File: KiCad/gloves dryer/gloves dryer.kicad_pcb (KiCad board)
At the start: 2 copper layers, 36 x 40 mm, 21 parts, among them J1 Conn_01x03, J4 PJ-114AH-SMT-TR, J5 Conn_01x02, J6 Conn_01x05, J7 Conn_01x02, Q1 PN2222A, Q2 PN2222A, SW1 SW_Push_Dual, SW2 SW_Push_Dual, U1 PIC16F18126-I/P, U2 AMS1117-5.0

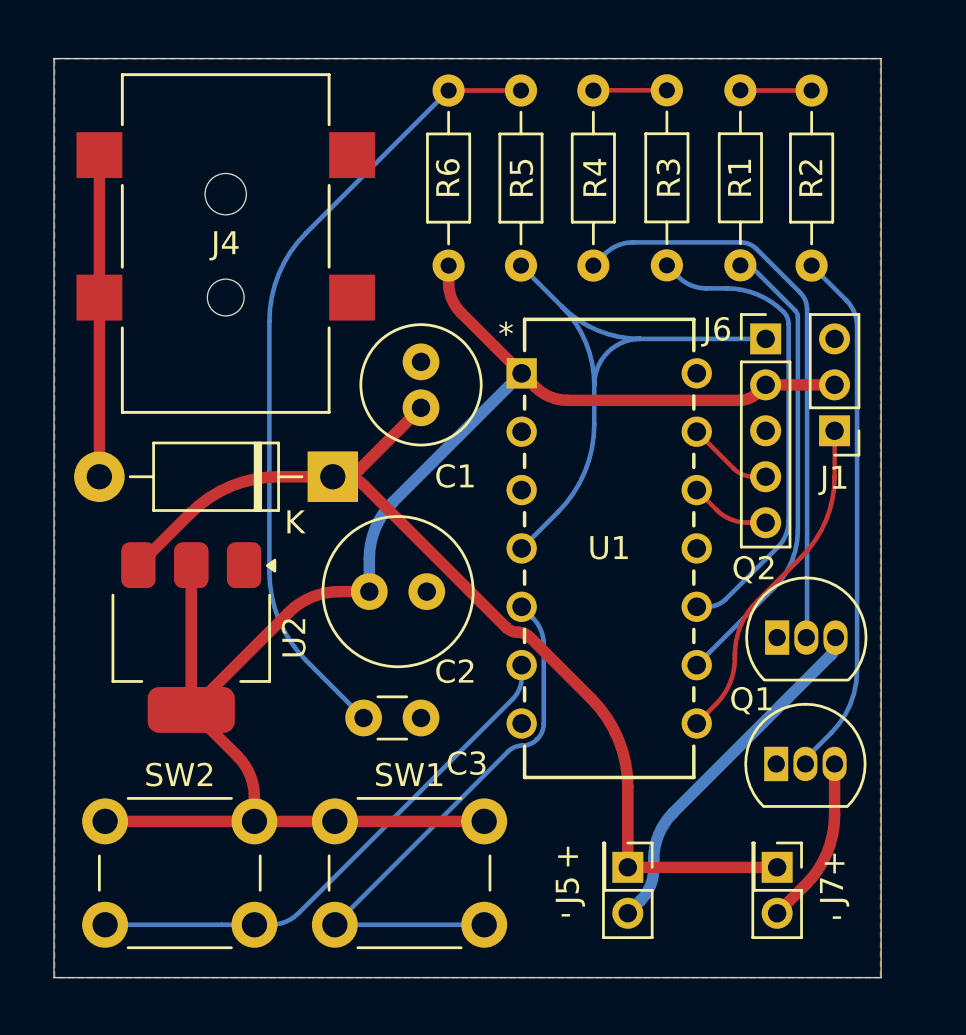
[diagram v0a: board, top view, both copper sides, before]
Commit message: Finished PCB, working on firmware for added switch state
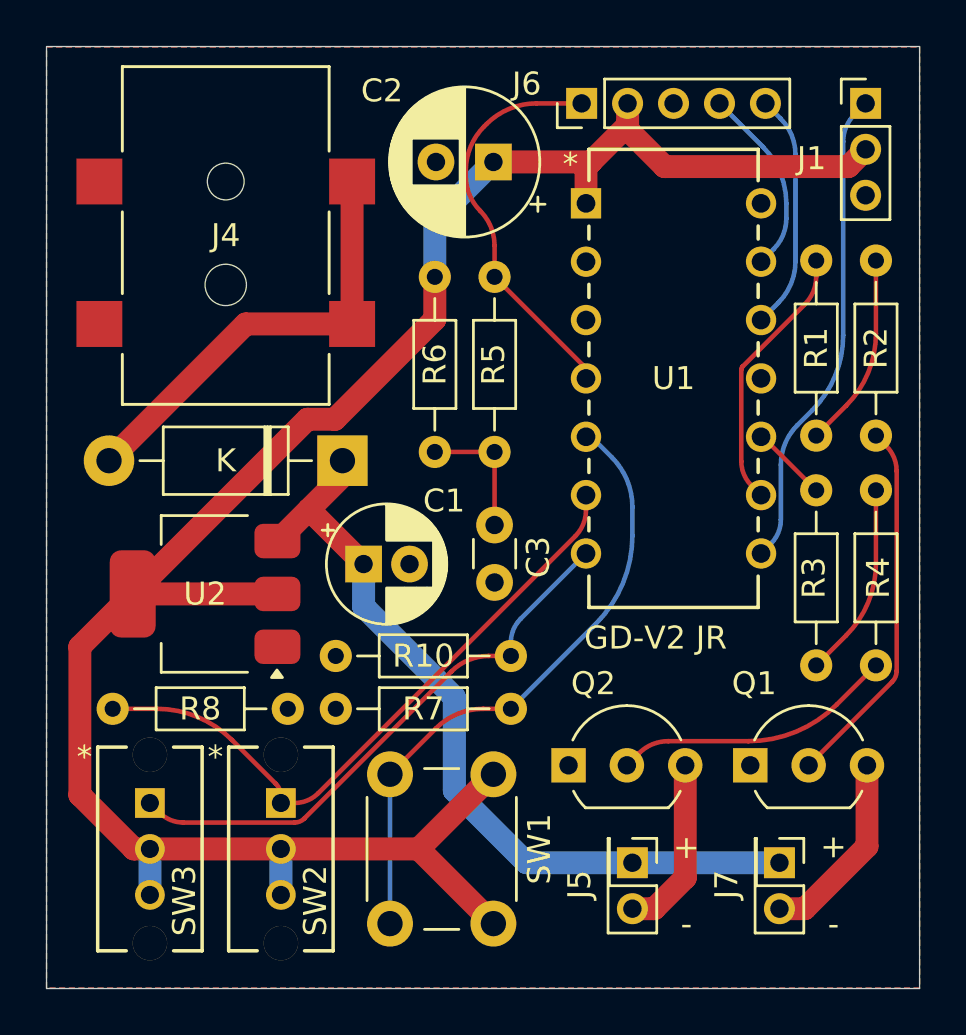
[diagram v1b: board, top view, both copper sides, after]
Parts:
- added R10: 10k, Resistor_THT:R_Axial_DIN0204_L3.6mm_D1.6mm_P7.62mm_Horizontal, F.Cu at (173.8, 76.8)
- added R7: 10k, Resistor_THT:R_Axial_DIN0204_L3.6mm_D1.6mm_P7.62mm_Horizontal, F.Cu at (173.8, 79.1)
- added R8: 10k, Resistor_THT:R_Axial_DIN0204_L3.6mm_D1.6mm_P7.62mm_Horizontal, F.Cu at (171.7, 79.1)
- added SW3: OS102011MS2QN1, OS102011MS2QN1:SPDT_OS102011_CNK, F.Cu at (165.7, 83.2)
- C1: footprint Capacitor_THT:C_Radial_D5.0mm_H11.0mm_P2.00mm -> Capacitor_THT:CP_Radial_D5.0mm_P2.00mm
- C2: footprint Capacitor_THT:C_Radial_D6.3mm_H11.0mm_P2.50mm -> Capacitor_THT:CP_Radial_D6.3mm_P2.50mm
- Q1, Q2: footprint Package_TO_SOT_THT:TO-92_Inline -> Package_TO_SOT_THT:TO-92_Inline_Wide
- SW2: value SW_Push_Dual -> OS102011MS2QN1; footprint Button_Switch_THT:SW_PUSH_6mm_H5mm -> OS102011MS2QN1:SPDT_OS102011_CNK
- moved R4 21.3 mm to (197.3, 69.6)
- moved C2 19.5 mm to (180.7, 55.3), turned to 180 degrees
- moved R5 15.8 mm to (180.7, 67.9), turned to 90 degrees
- moved R6 15.7 mm to (178.1, 67.9), turned to 90 degrees
- moved J1 14.3 mm to (196.8, 52.8), turned to 0 degrees
- moved J6 13.0 mm to (184.5, 52.8), turned to 90 degrees
- moved R3 11.8 mm to (194.7, 69.6), turned to -90 degrees
- moved Q2 10.6 mm to (183.9, 81.6)
- moved C3 10.2 mm to (180.7, 71.1), turned to -90 degrees
- moved R2 7.91 mm to (197.3, 59.6)
- moved U1 7.91 mm to (184.7, 57.1)
- moved SW2 7.69 mm to (171.4, 83.2)
- moved C1 7.24 mm to (175.0, 72.8), turned to 0 degrees
- moved SW1 7.20 mm to (180.6, 82.0), turned to -90 degrees
- moved R1 3.31 mm to (194.7, 59.6), turned to -90 degrees
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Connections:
- SW2 pad 1: /VDD_5V -> /SW1
- SW2 pad 2: /BT2 -> /VDD_5V
- U1 pad 6: /BT2 -> /SW1
- U1 pad 7: unconnected-(U1-RC3-Pad7) -> /SW2
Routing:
- net Net-(C3-Pad1): track 34.9 -> 5.78 mm
- net /SW1: track 0.00 -> 28.4 mm
- net /SW2: track 0.00 -> 24.6 mm
- net /BT2: track 23.3 -> 0.00 mm
- net /VDD_5V: track 70.6 -> 91.8 mm
- net /IF1: track 20.6 -> 3.36 mm
- net Net-(Q2-B): track 25.3 -> 12.3 mm
- net /VDDG_12V: track 45.0 -> 35.0 mm
- net /MCLR: track 26.7 -> 17.6 mm
- net /IF2: track 20.3 -> 11.8 mm
- net /F1-: track 15.5 -> 7.75 mm
- net Net-(Q1-B): track 23.2 -> 16.2 mm
- net /CLK: track 3.50 -> 10.4 mm
- net /IO_SENS: track 14.7 -> 21.0 mm
- net /VDD_12V: track 14.2 -> 19.8 mm
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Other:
- board size 36 x 40 mm -> 38 x 41 mm
- board text added: "GD-V2 JR"

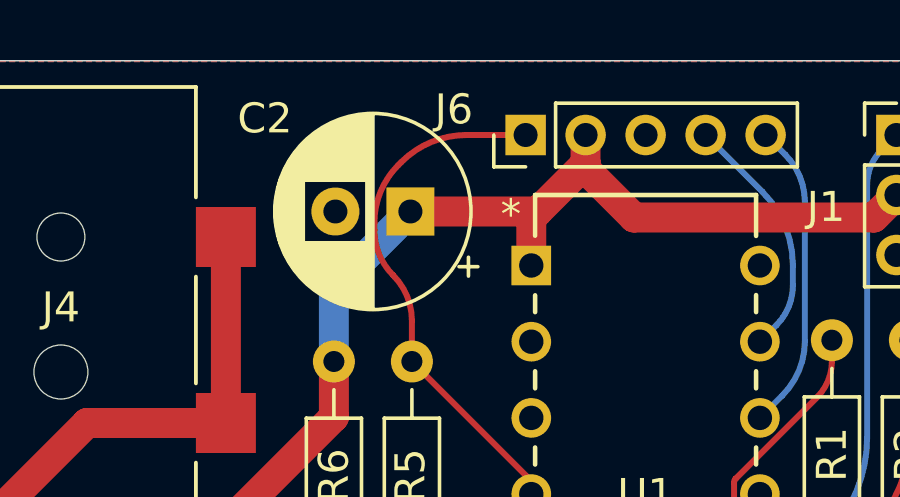
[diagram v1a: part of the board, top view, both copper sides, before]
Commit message: Updated firmware for version two of the project, as well as kicad file for version 2
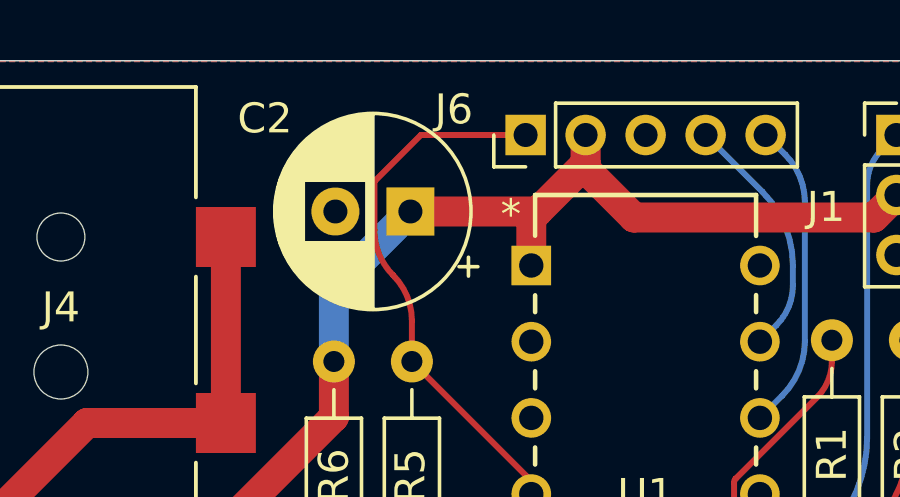
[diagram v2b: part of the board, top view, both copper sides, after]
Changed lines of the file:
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@@
 	)
 	(segment
-		(start 182.522792 52.75)
-		(end 184.49 52.75)
+		(start 181 52.75)
+		(end 179.45 54.3)
+		(width 0.2)
+		(layer "F.Cu")
+		(net 20)
+	)
+	(segment
+		(start 184.68 64.5)
+		(end 184.68 64.72)
 		(width 0.2)
 		(layer "F.Cu")
@@
 	)
 	(segment
-		(start 184.68 64.5)
-		(end 184.68 64.72)
+		(start 184.49 52.75)
+		(end 181 52.75)
 		(width 0.2)
 		(layer "F.Cu")
@@
 	)
 	(segment
-		(start 180.245495 53.754504)
-		(end 180.35 53.65)
-		(width 0.2)
-		(layer "F.Cu")
-		(net 20)
-	)
-	(segment
-		(start 179.45 55.916116)
-		(end 179.45 55.675)
+		(start 179.45 54.3)
+		(end 179.45 55.916116)
 		(width 0.2)
 		(layer "F.Cu")
@@
 	)
 	(arc
+		(start 180.075 57.425)
+		(mid 180.537567 58.117281)
+		(end 180.7 58.933883)
+		(width 0.2)
+		(layer "F.Cu")
+		(net 20)
+	)
+	(arc
 		(start 179.45 55.916116)
 		(mid 179.612432 56.732718)
@@
 		(width 0.2)
 		(layer "F.Cu")
-		(net 20)
-	)
-	(arc
-		(start 180.245495 53.754504)
-		(mid 179.656742 54.635635)
-		(end 179.45 55.675)
-		(width 0.2)
-		(layer "F.Cu")
-		(net 20)
-	)
-	(arc
-		(start 182.522792 52.75)
-		(mid 181.346885 52.983902)
-		(end 180.35 53.65)
-		(width 0.2)
-		(layer "F.Cu")
-		(net 20)
-	)
-	(arc
-		(start 180.075 57.425)
-		(mid 180.537567 58.117281)
-		(end 180.7 58.933883)
-		(width 0.2)
-		(layer "F.Cu")
